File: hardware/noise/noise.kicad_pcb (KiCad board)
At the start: 2 copper layers, 42 x 100 mm, 65 parts, among them J1 Conn_02x05_Odd_Even, J2 White, J3 Pink, J4 Blue, J5 Grainy, J6 HP Grainy, Q1 BC547, U1 TL074, U2 TL072

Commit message: finished design checks on grain output and update schematic/layout to v1.1
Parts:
- added RV3: 50k, Potentiometer_THT:Potentiometer_Piher_PT-6-V_Vertical, F.Cu at (135.2, 126.0)
- C12, C6: value 100n -> 10n; footprint Capacitor_THT:C_Rect_L13.0mm_W4.0mm_P10.00mm_FKS3_FKP3_MKS4 -> Capacitor_THT:C_Rect_L7.0mm_W3.5mm_P5.00mm
- C13, C7: value 10n -> 2n2
- C14, C8: value 2n2 -> 470p; footprint Capacitor_THT:C_Rect_L7.0mm_W3.5mm_P5.00mm -> Capacitor_THT:C_Disc_D4.7mm_W2.5mm_P5.00mm
- C5: value 100n -> 1u
- J2, J3, J4, J5, J6: footprint AudioJacks:Jack_3.5mm_QingPu_WQP-PJ316M_Horizontal_1 -> AudioJacks:Jack_3.5mm_QingPu_WQP-PJ323M_Horizontal
- R10, R21: value 22k -> 68k
- R11, R22: value 3k3 -> 15k
- R18: value 33k -> 68k
- R20, R9: value 150k -> 330k
- R27: value 220k -> 100k
- R28: value 47k -> 120k
- R29: value 47k -> 100k
- R5, R7: value 10k -> 22k
- R8: value 100k -> 150k
- RV1: value 500k -> 470k
- moved C8 4.29 mm to (134.7, 65.0)
- moved R11 4.29 mm to (137.4, 65.0)
- moved C6 4.29 mm to (134.7, 56.6)
- moved R9 4.28 mm to (137.4, 56.6)
- moved C7 4.09 mm to (134.7, 60.7)
- moved R10 4.09 mm to (137.4, 60.7)
- moved R29 2.63 mm to (135.2, 118.7), turned to 90 degrees
- moved D3 2.38 mm to (137.8, 111.1)
- moved C22 0.54 mm to (132.1, 125.0), turned to 180 degrees
- moved C12 0.25 mm to (122.0, 65.0)
- moved J2 0.20 mm to (101.7, 62.5)
- moved J3 0.20 mm to (101.7, 77.5)
- moved J4 0.20 mm to (101.7, 92.5)
- moved J5 0.20 mm to (101.7, 107.5)
- moved J6 0.20 mm to (101.7, 122.5)
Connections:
- R29 pad 1: Net-(U2B--) -> Net-(R29-Pad1)
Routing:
- net Net-(U2B--): track 50.1 -> 62.2 mm
- net Net-(R29-Pad1): track 0.00 -> 8.51 mm
- net Net-(U1C-+): track 33.4 -> 26.5 mm
- net Net-(U2A--): track 38.6 -> 33.2 mm
- net Net-(D3-A): track 15.0 -> 19.0 mm, vias 0 -> 1
- net Net-(C12-Pad2): track 91.2 -> 88.2 mm
- net Net-(D3-K): track 24.1 -> 22.7 mm
- net -12V: track 79.6 -> 80.4 mm
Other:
- board text added: "v1.1.20250308"
- board text removed: "v1.0.20250207"

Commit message: Submitted board v1.1 for fab
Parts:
- moved R1 16.0 mm to (130.0, 129.7), turned to 180 degrees
- moved C2 15.6 mm to (120.4, 142.8), turned to 90 degrees
- moved R2 10.1 mm to (130.0, 147.5), turned to 180 degrees
- moved J1 7.24 mm to (138.3, 143.8), turned to 180 degrees
- moved C21 7.17 mm to (124.9, 140.2), turned to 0 degrees
- moved C1 6.44 mm to (115.6, 133.2), turned to -90 degrees
- moved D1 5.98 mm to (129.3, 143.8), turned to 180 degrees
- moved C18 1.90 mm to (125.0, 136.8), turned to 180 degrees
- moved D2 1.23 mm to (120.7, 133.2), turned to 0 degrees
- moved R5 0.20 mm to (121.9, 97.0)
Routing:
- net -12V: track 80.4 -> 94.0 mm
- net Net-(D2-A): track 11.3 -> 6.15 mm
- net +12V: track 77.8 -> 82.6 mm
- net Net-(J1-Pin_10): track 9.06 -> 9.95 mm
- net Net-(J1-Pin_1): track 9.06 -> 9.84 mm

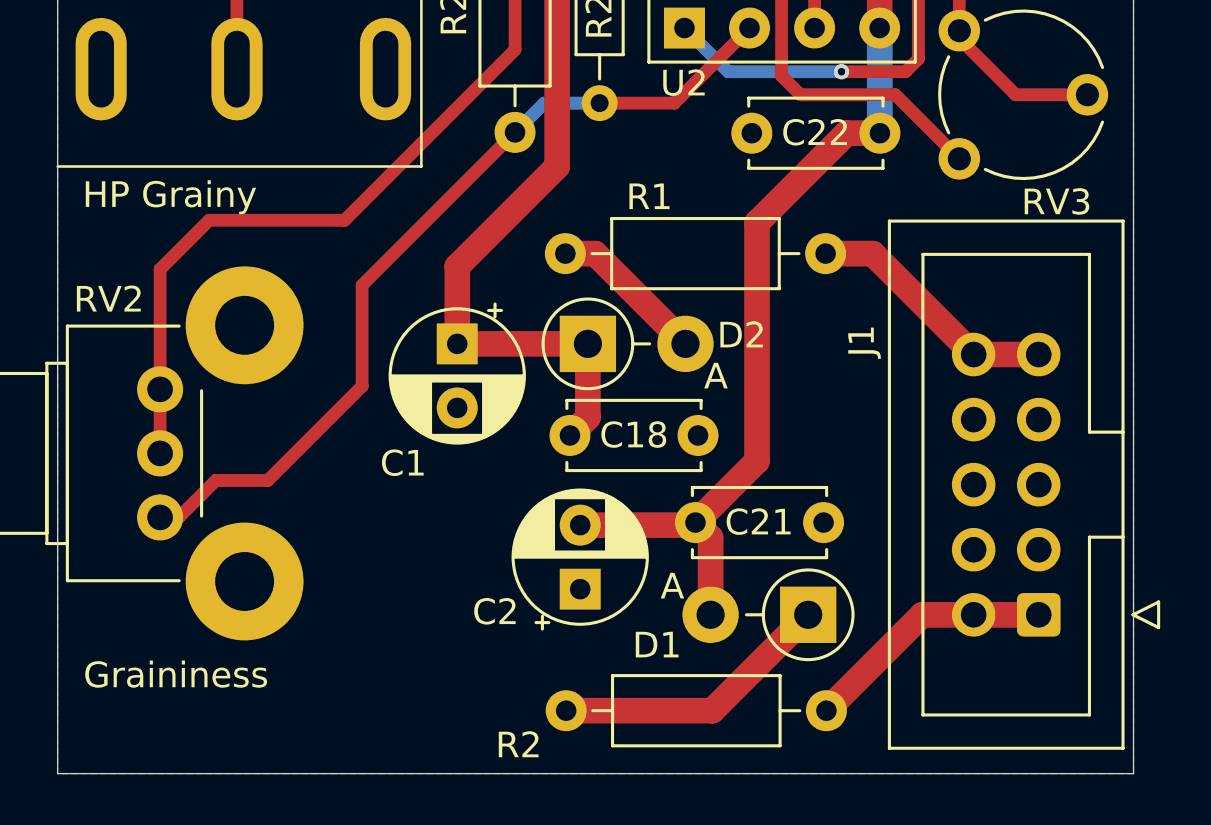
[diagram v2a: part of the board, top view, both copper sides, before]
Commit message: Fixed bad orientation for IDC header to support horizontal and vertical plugs
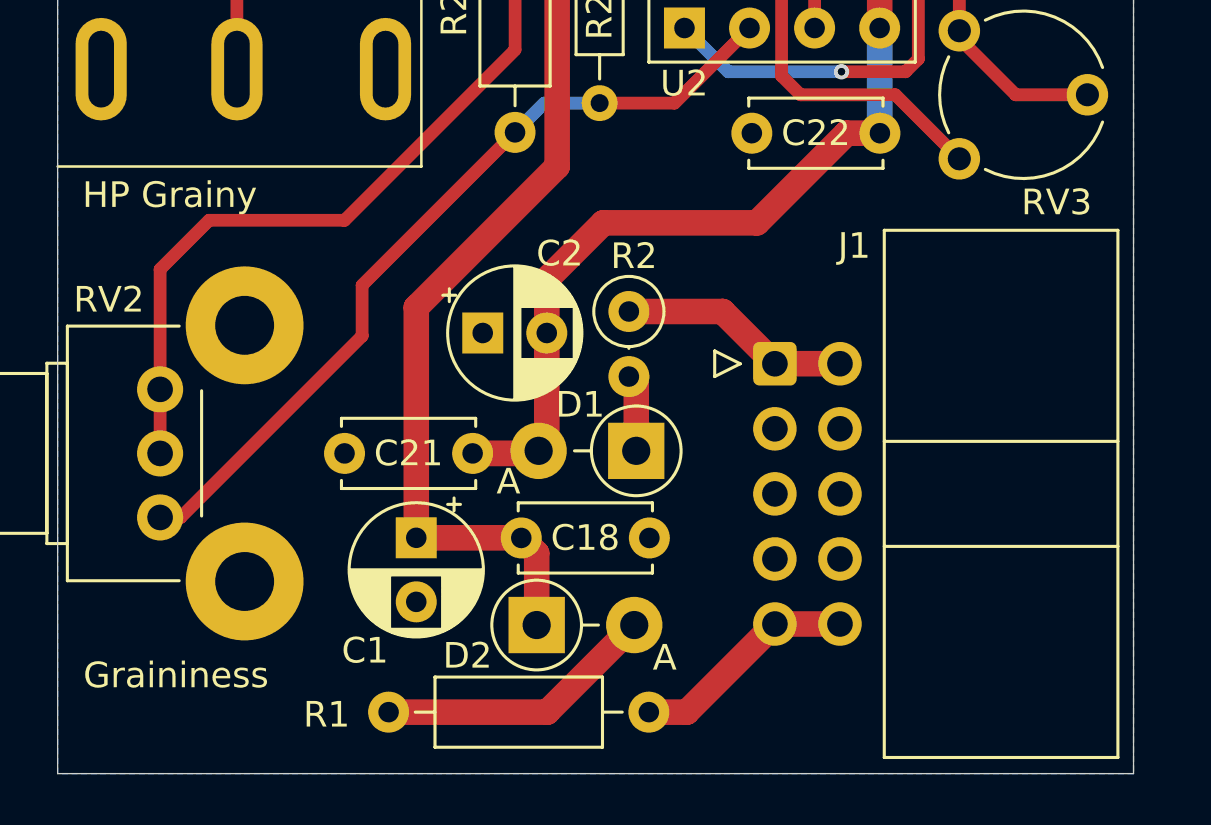
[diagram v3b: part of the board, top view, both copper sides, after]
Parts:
- J1: footprint Connector_IDC:IDC-Header_2x05_P2.54mm_Vertical -> Connector_IDC:IDC-Header_2x05_P2.54mm_Horizontal
- R2: footprint Resistor_THT:R_Axial_DIN0207_L6.3mm_D2.5mm_P10.16mm_Horizontal -> Resistor_THT:R_Axial_DIN0207_L6.3mm_D2.5mm_P2.54mm_Vertical
- moved R1 19.2 mm to (123.1, 147.6)
- moved R2 17.4 mm to (122.3, 132.0), turned to -90 degrees
- moved J1 14.2 mm to (128.0, 134.0), turned to 0 degrees
- moved D2 11.2 mm to (118.7, 144.2)
- moved C2 10.7 mm to (116.6, 132.8), turned to 0 degrees
- moved D1 9.27 mm to (122.6, 137.4)
- moved C21 9.11 mm to (116.2, 137.5), turned to 180 degrees
- moved C1 7.74 mm to (114.0, 140.8)
- moved C18 4.43 mm to (123.1, 140.8)
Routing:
- net Net-(D1-K): track 11.0 -> 3.32 mm
- net +12V: track 82.6 -> 89.6 mm
- net Net-(D2-A): track 6.15 -> 11.0 mm
- net -12V: track 94.0 -> 91.5 mm
- net Net-(U2A--): track 33.2 -> 32.1 mm
- net Net-(J1-Pin_10): track 9.95 -> 8.88 mm
- net Net-(J1-Pin_1): track 9.84 -> 8.78 mm
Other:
- board text added: "v1.2.20250312"
- board text removed: "v1.1.20250308"

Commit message: PCB silk tidy-up and added faceplate
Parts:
- moved R25 2.28 mm to (136.9, 102.5)
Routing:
- net Net-(U2A-+): track 24.8 -> 23.9 mm
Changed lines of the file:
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@@
 		)
 		(property "Value" "10u"
-			(at 1.25 3.75 360)
+			(at 1.25 3.75 0)
 			(layer "F.Fab")
 			(effects
@@
 		)
 		(fp_text user "${REFERENCE}"
-			(at 1.25 0 360)
+			(at 1.25 0 0)
 			(layer "F.Fab")
 			(effects
@@
 		(tags "C Disc series Radial pin pitch 5.00mm  diameter 5mm width 2.5mm Capacitor")
 		(property "Reference" "C18"
-			(at 2.5 0 360)
+			(at 2.5 0 0)
 			(layer "F.SilkS")
 			(effects
@@
 		)
 		(property "Value" "100n"
-			(at 2.5 2.5 360)
+			(at 2.5 2.5 0)
 			(layer "F.Fab")
 			(effects
@@
 		)
 		(fp_text user "${REFERENCE}"
-			(at 2.5 0 360)
+			(at 2.5 0 0)
 			(layer "F.Fab")
 			(effects
@@
 		(tags "Diode DO-41_SOD81 series Axial Vertical pin pitch 3.81mm  length 5.2mm diameter 2.7mm")
 		(property "Reference" "D2"
-			(at -2.7 1.2 360)
+			(at -2.7 1.2 0)
 			(layer "F.SilkS")
 			(effects
@@
 		)
 		(property "Value" "D_Schottky"
-			(at 1.905 4.084135 360)
+			(at 1.905 4.084135 0)
 			(layer "F.Fab")
 			(effects
@@
 		)
 		(fp_text user "A"
-			(at 5 1.276 360)
+			(at 5 1.276 0)
 			(layer "F.SilkS")
 			(effects
@@
 		)
 		(fp_text user "A"
-			(at 2.01 1.1 360)
+			(at 2.01 1.1 0)
 			(layer "F.Fab")
 			(effects
@@
 		)
 		(fp_text user "${REFERENCE}"
-			(at 1.905 -2.750635 360)
+			(at 1.905 -2.750635 0)
 			(layer "F.Fab")
 			(effects
@@
 		(tags "C Disc series Radial pin pitch 5.00mm  diameter 5mm width 2.5mm Capacitor")
 		(property "Reference" "C21"
-			(at 2.5 0 360)
+			(at 2.5 0 0)
 			(layer "F.SilkS")
 			(effects
@@
 		)
 		(property "Value" "100n"
-			(at 2.5 2.5 360)
+			(at 2.5 2.5 0)
 			(layer "F.Fab")
 			(effects
@@
 		)
 		(fp_text user "${REFERENCE}"
-			(at 2.5 0 360)
+			(at 2.5 0 0)
 			(layer "F.Fab")
 			(effects
@@
 		(tags "Diode DO-41_SOD81 series Axial Vertical pin pitch 3.81mm  length 5.2mm diameter 2.7mm")
 		(property "Reference" "D1"
-			(at 2.187183 1.8 360)
+			(at 2.187183 1.8 0)
 			(layer "F.SilkS")
 			(effects
@@
 		)
 		(property "Value" "D_Schottky"
-			(at 1.905 4.084135 360)
+			(at 1.905 4.084135 0)
 			(layer "F.Fab")
 			(effects
@@
 		)
 		(fp_text user "A"
-			(at 4.987183 -1.2 360)
+			(at 4.987183 -1.2 0)
 			(layer "F.SilkS")
 			(effects
@@
 		)
 		(fp_text user "A"
-			(at 2.01 1.1 360)
+			(at 2.01 1.1 0)
 			(layer "F.Fab")
 			(effects
@@
 		)
 		(fp_text user "${REFERENCE}"
-			(at 1.905 -2.750635 360)
+			(at 1.905 -2.750635 0)
 			(layer "F.Fab")
 			(effects
@@
 	(footprint "Resistor_THT:R_Axial_DIN0204_L3.6mm_D1.6mm_P2.54mm_Vertical"
 		(layer "F.Cu")
-		(at 134.62 102.412 -90)
+		(at 136.9 102.48 -90)
 		(descr "Resistor, Axial_DIN0204 series, Axial, Vertical, pin pitch=2.54mm, 0.167W, length*diameter=3.6*1.6mm^2, http://cdn-reichelt.de/documents/datenblatt/B400/1_4W%23YAG.pdf")
 		(tags "Resistor Axial_DIN0204 series Axial Vertical pin pitch 2.54mm 0.167W length 3.6mm diameter 1.6mm")
@@
 		(tags "CP Radial series Radial pin pitch 2.50mm  diameter 5mm Electrolytic Capacitor")
 		(property "Reference" "C1"
-			(at 4.405113 2 360)
+			(at 4.405113 2 0)
 			(layer "F.SilkS")
 			(effects
@@
 	)
 	(segment
-		(start 134.869 88.128)
-		(end 136.248 88.128)
-		(width 0.5)
-		(layer "F.Cu")
-		(net 17)
-	)
-	(segment
-		(start 132.294 104.862)
-		(end 132.294 104.434)
+		(start 136.9 102.48)
+		(end 138.684 100.696)
 		(width 0.5)
 		(layer "F.Cu")
@@
 	)
 	(segment
-		(start 134.62 102.412)
-		(end 137.11 102.412)
+		(start 115.48 54.61)
+		(end 112.98 57.11)
 		(width 0.5)
 		(layer "F.Cu")
@@
 	)
 	(segment
-		(start 115.48 54.61)
-		(end 112.98 57.11)
+		(start 138.684 100.696)
+		(end 138.684 89.408)
 		(width 0.5)
 		(layer "F.Cu")
@@
 	)
 	(segment
-		(start 136.248 88.128)
-		(end 136.258 88.138)
+		(start 132.294 104.862)
+		(end 132.294 104.434)
 		(width 0.5)
 		(layer "F.Cu")
@@
 	)
 	(segment
-		(start 136.258 88.138)
+		(start 138.684 89.408)
 		(end 137.414 88.138)
 		(width 0.5)
@@
 	)
 	(segment
-		(start 134.316 102.412)
-		(end 134.62 102.412)
+		(start 136.832 102.412)
+		(end 136.9 102.48)
+		(width 0.5)
+		(layer "F.Cu")
+		(net 17)
+	)
+	(segment
+		(start 137.414 88.138)
+		(end 136.258 88.138)
 		(width 0.5)
 		(layer "F.Cu")
@@
 	)
 	(segment
-		(start 127 65.024)
-		(end 127 68.784)
+		(start 136.248 88.128)
+		(end 134.869 88.128)
 		(width 0.5)
 		(layer "F.Cu")
@@
 	)
 	(segment
-		(start 138.684 89.408)
-		(end 138.684 100.838)
+		(start 127 65.024)
+		(end 127 68.784)
 		(width 0.5)
 		(layer "F.Cu")
@@
 	)
 	(segment
-		(start 124.928 54.61)
-		(end 126.96 56.642)
+		(start 136.258 88.138)
+		(end 136.248 88.128)
 		(width 0.5)
 		(layer "F.Cu")
@@
 	)
 	(segment
-		(start 137.414 88.138)
-		(end 138.684 89.408)
+		(start 132.294 104.434)
+		(end 134.316 102.412)
 		(width 0.5)
 		(layer "F.Cu")
@@
 	)
 	(segment
-		(start 132.294 104.434)
-		(end 134.316 102.412)
+		(start 124.928 54.61)
+		(end 126.96 56.642)
 		(width 0.5)
 		(layer "F.Cu")
@@
 	)
 	(segment
-		(start 137.11 102.412)
-		(end 138.684 100.838)
+		(start 134.316 102.412)
+		(end 136.832 102.412)
 		(width 0.5)
 		(layer "F.Cu")
@@
 	)
 	(segment
-		(start 129.55 118.55)
-		(end 134.2 113.9)
+		(start 134.2 113.9)
+		(end 138.5 113.9)
 		(width 0.5)
 		(layer "F.Cu")
@@
 	)
 	(segment
-		(start 139.7508 110.0828)
-		(end 134.62 104.952)
+		(start 129.55 118.55)
+		(end 134.2 113.9)
 		(width 0.5)
 		(layer "F.Cu")
@@
 	)
 	(segment
-		(start 134.2 113.9)
-		(end 138.5 113.9)
+		(start 139.7508 112.6492)
+		(end 139.7508 107.8708)
 		(width 0.5)
 		(layer "F.Cu")
@@
 	)
 	(segment
-		(start 138.5 113.9)
-		(end 139.7508 112.6492)
+		(start 129.55 120.894)
+		(end 129.55 118.55)
 		(width 0.5)
 		(layer "F.Cu")
@@
 	)
 	(segment
-		(start 139.7508 112.6492)
-		(end 139.7508 110.0828)
+		(start 138.5 113.9)
+		(end 139.7508 112.6492)
 		(width 0.5)
 		(layer "F.Cu")
@@
 	)
 	(segment
-		(start 129.55 120.894)
-		(end 129.55 118.55)
+		(start 139.7508 107.8708)
+		(end 136.832 104.952)
 		(width 0.5)
 		(layer "F.Cu")
